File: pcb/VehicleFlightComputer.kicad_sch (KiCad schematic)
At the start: 55 parts, among them J1 FFC2B28-24-G, J3 USB_C_Receptacle, J4 Debug, Q1 S8050, SW1 B3U-1000P, U1 STM32H533VET6, U2 LIS2MDL, U3 LSM6DSV32X, U4 MCP2221A-I/ST, U5 AP2112K-3.3

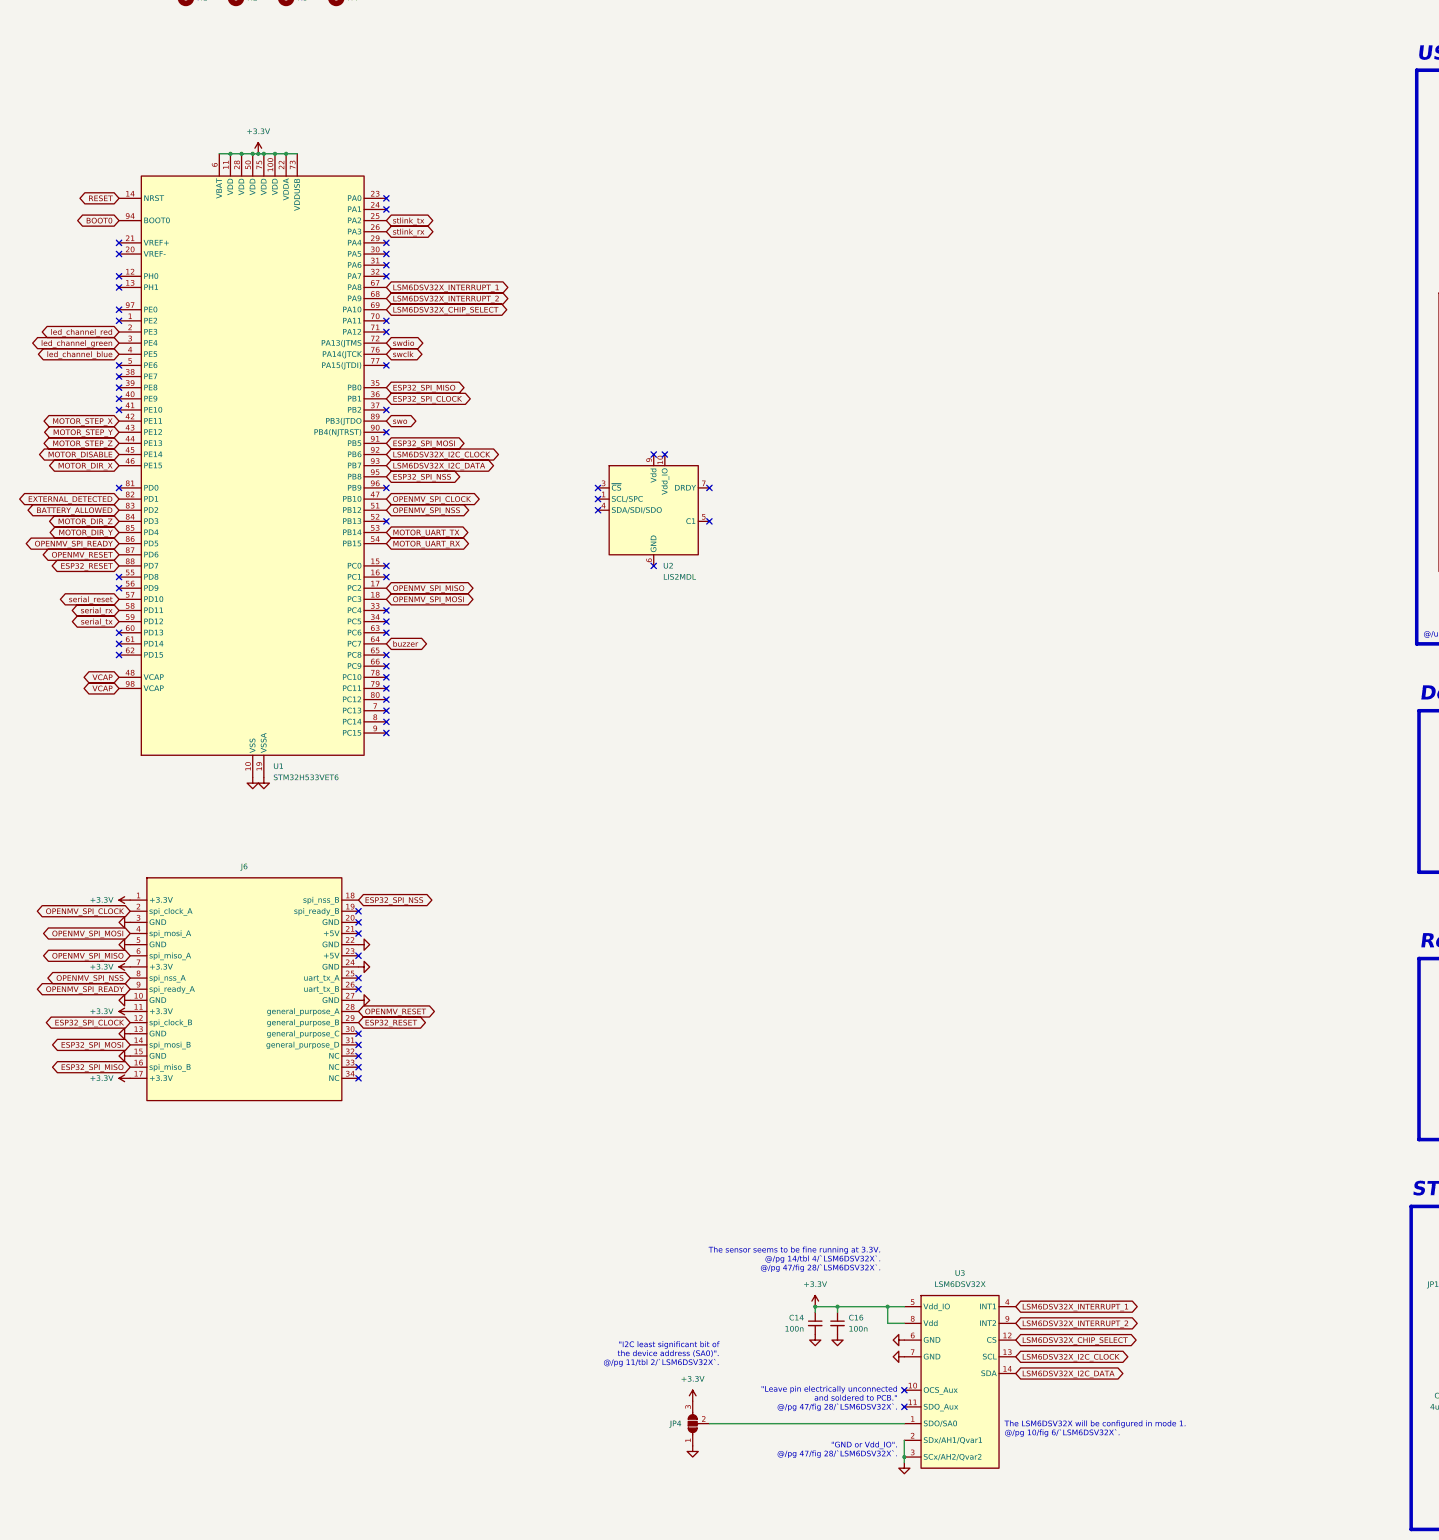
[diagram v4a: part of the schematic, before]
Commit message: Set up schematic for LIS2MDL on `VehicleFlightComputer`.
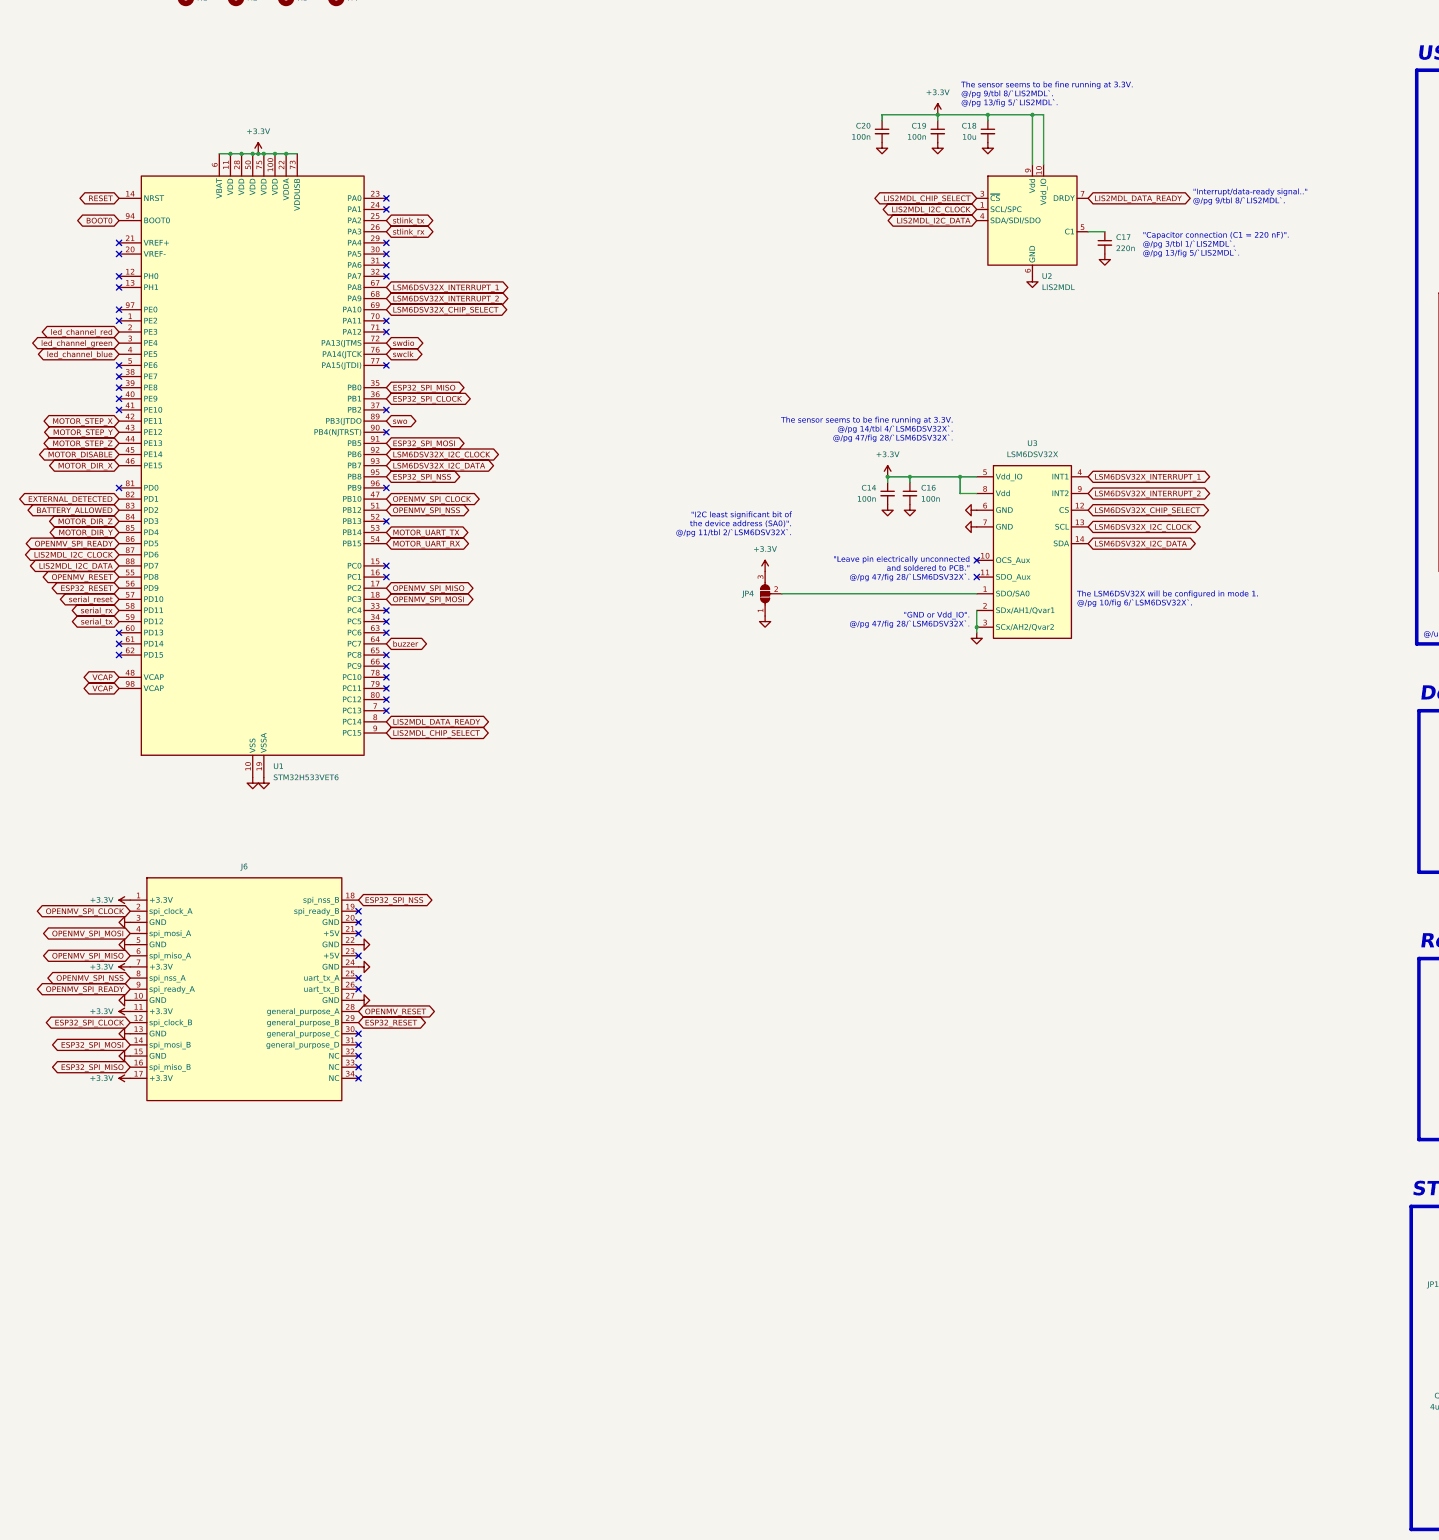
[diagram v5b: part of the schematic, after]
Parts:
- added C17: 220n, Capacitor_SMD:C_1206_3216Metric_Pad1.33x1.80mm_HandSolder, symbol Device:C_Small
- added C18: 10u, Capacitor_SMD:C_1206_3216Metric_Pad1.33x1.80mm_HandSolder, symbol Device:C_Small
- added C19, C20: 100n, Capacitor_SMD:C_1206_3216Metric_Pad1.33x1.80mm_HandSolder, symbol Device:C_Small
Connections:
- net +3.3V: now also U2.10 (Vdd_IO), U2.9 (Vdd), C18.1, C19.1, C20.1
- net ESP32_RESET: now also U1.56 (PD9); no longer U1.88 (PD7)
- net GND: now also U2.6 (GND), U2.8 (GND), C17.2, C18.2, C19.2, C20.2
- net OPENMV_RESET: now also U1.55 (PD8); no longer U1.87 (PD6)
- net LIS2MDL_I2C_CLOCK: now reaches U2.1 (SCL/SPC)
- net LIS2MDL_I2C_CLOCK: now also U1.87 (PD6)
- net LIS2MDL_CHIP_SELECT: now reaches U2.3 (~{CS})
- net LIS2MDL_CHIP_SELECT: now also U1.9 (PC15)
- net LIS2MDL_I2C_DATA: now reaches U2.4 (SDA/SDI/SDO)
- net LIS2MDL_I2C_DATA: now also U1.88 (PD7)
- net at U2.5 (C1): now also C17.1
- net LIS2MDL_DATA_READY: now reaches U2.7 (DRDY)
- net LIS2MDL_DATA_READY: now also U1.8 (PC14)
- no-connect marks 79 -> 67
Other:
- note added: ""Capacitor connection (C1 = 220 nF)". @/pg 3/tbl 1/`LIS2MDL`. @/pg 13/fig 5/`LIS2MDL`."
- note added: ""Interrupt/data-ready signal.." @/pg 9/tbl 8/`LIS2MDL`."
- note added: "The sensor seems to be fine running at 3.3V. @/pg 9/tbl 8/`LIS2MDL`. @/pg 13/fig 5/`LIS2MDL`."
- moved on the sheet: C14, C16, JP4, U2, U3

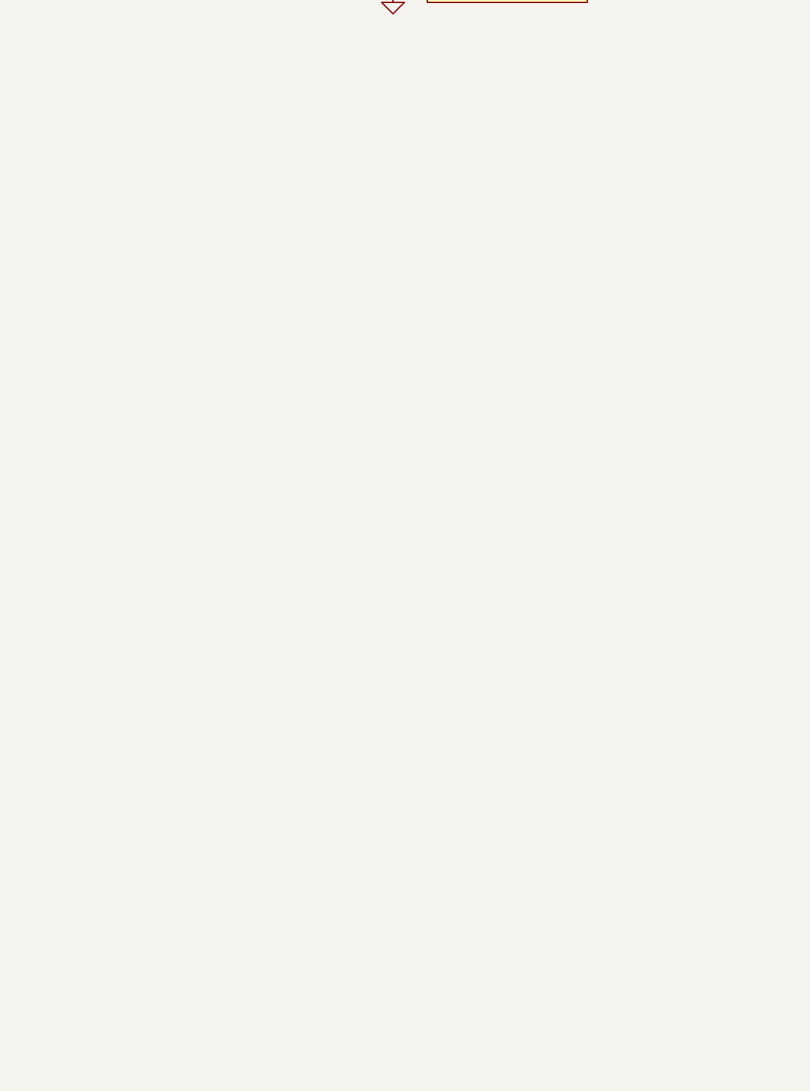
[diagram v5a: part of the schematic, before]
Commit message: Added pull-ups on `VehicleFlightComputer`.
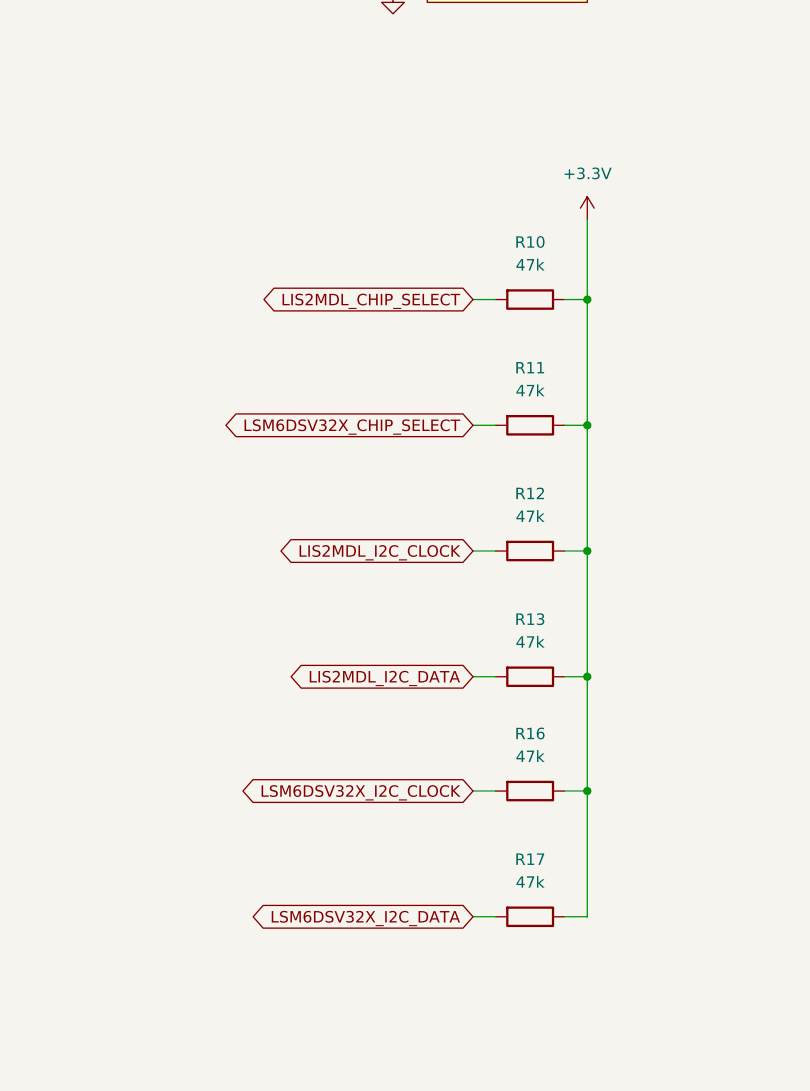
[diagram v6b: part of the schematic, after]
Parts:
- added R10, R11, R12, R13, R16, R17: 47k, Resistor_SMD:R_1206_3216Metric_Pad1.30x1.75mm_HandSolder, symbol Device:R
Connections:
- net +3.3V: now also R10.1, R11.1, R12.1, R13.1, R16.1, R17.1
- net LIS2MDL_CHIP_SELECT: now also R10.2
- net LIS2MDL_I2C_CLOCK: now also R12.2
- net LIS2MDL_I2C_DATA: now also R13.2
- net LSM6DSV32X_CHIP_SELECT: now also R11.2
- net LSM6DSV32X_I2C_CLOCK: now also R16.2
- net LSM6DSV32X_I2C_DATA: now also R17.2

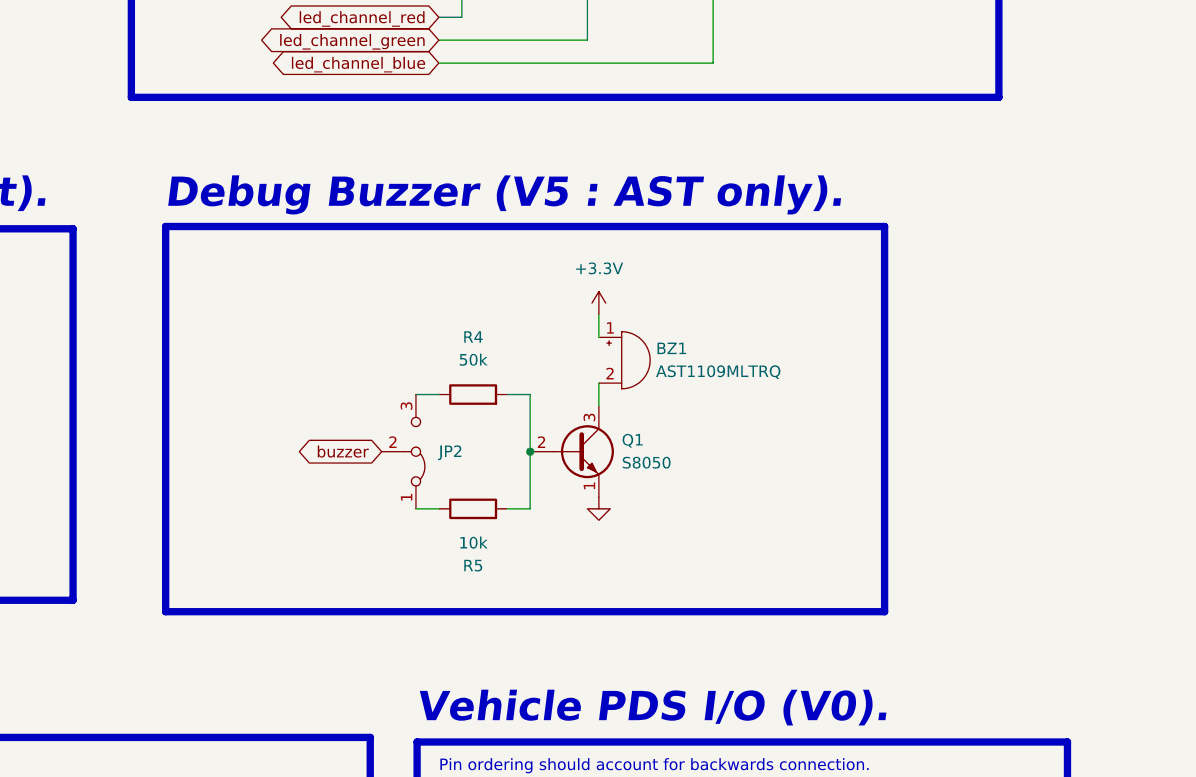
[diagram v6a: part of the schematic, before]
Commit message: Rough layout of footprints for `VehicleFlightComputer`.
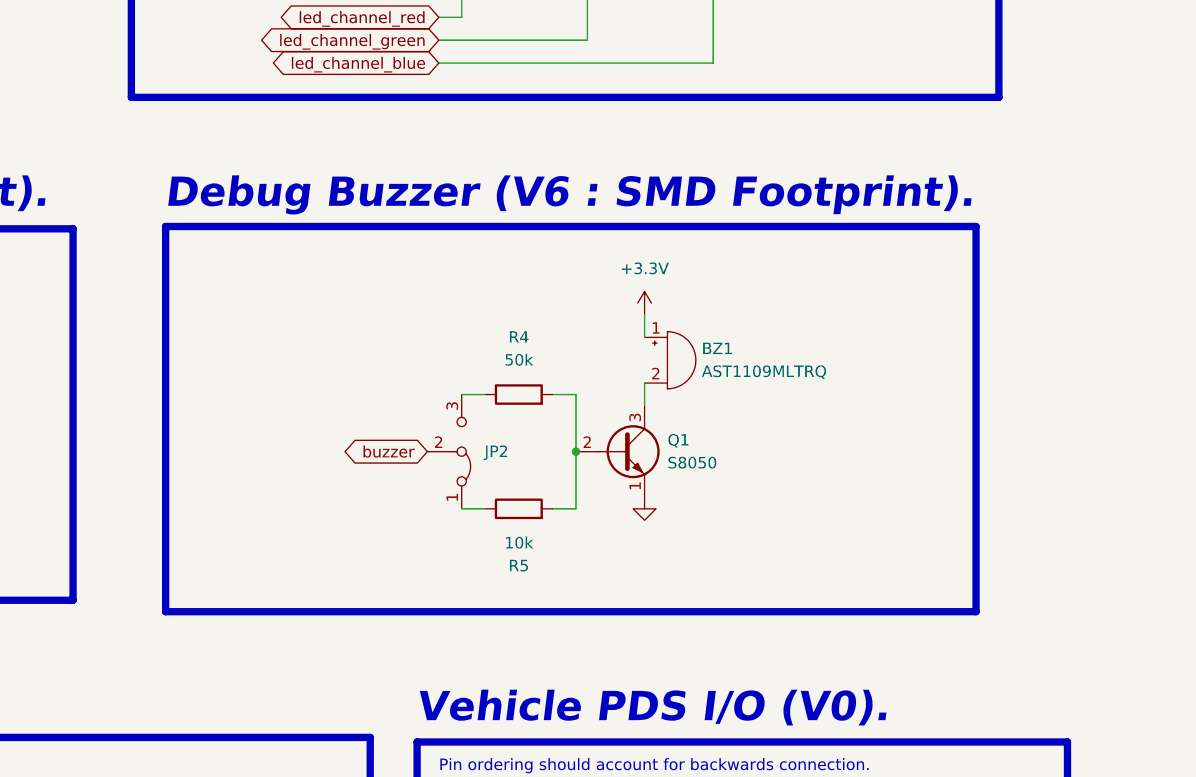
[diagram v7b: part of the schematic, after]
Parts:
- Q1: footprint Package_TO_SOT_THT:TO-92_Inline -> Package_TO_SOT_SMD:SOT-23_Handsoldering
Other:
- note added: "Debug Buzzer (V6 : SMD Footprint)."
- note removed: "Debug Buzzer (V5 : AST only)."
- moved on the sheet: BZ1, JP2, Q1, R4, R5
